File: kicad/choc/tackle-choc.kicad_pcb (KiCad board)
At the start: 2 copper layers, 158 x 119 mm, 114 parts, among them J1 Conn_01x02, SW1 SW_Push, SW10 SW_Push, SW11 SW_Push, SW12 SW_Push, SW13 SW_Push, SW14 SW_Push, SW15 SW_Push, SW16 SW_Push, SW17 SW_Push, SW18 SW_Push, SW19 SW_Push, SW2 SW_Push, SW20 SW_Push, SW21 SW_Push, SW22 SW_Push, SW23 SW_Push, SW24 SW_Push, SW25 SW_Push, SW26 SW_Push, SW27 SW_Push, SW28 SW_Push, SW29 SW_Push, SW3 SW_Push, SW30 SW_Push, SW31 SW_Push, SW32 SW_Push, SW33 SW_Push, SW34 SW_Push, SW35 SW_Push, SW36 SW_Push, SW37 SW_Push, SW38 SW_Push, SW39 SW_Push, SW4 SW_Push, SW40 SW_Push, SW41 SW_Push, SW42 SW_Push, SW43 SW_Push, SW44 SW_Push, SW45 SW_Push, SW46 SW_Push, SW47 SW_Push, SW48 SW_Push, SW5 SW_Push, SW6 SW_Push, SW7 SW_Push, SW8 SW_Push, SW9 SW_Push, U1 nice!nano

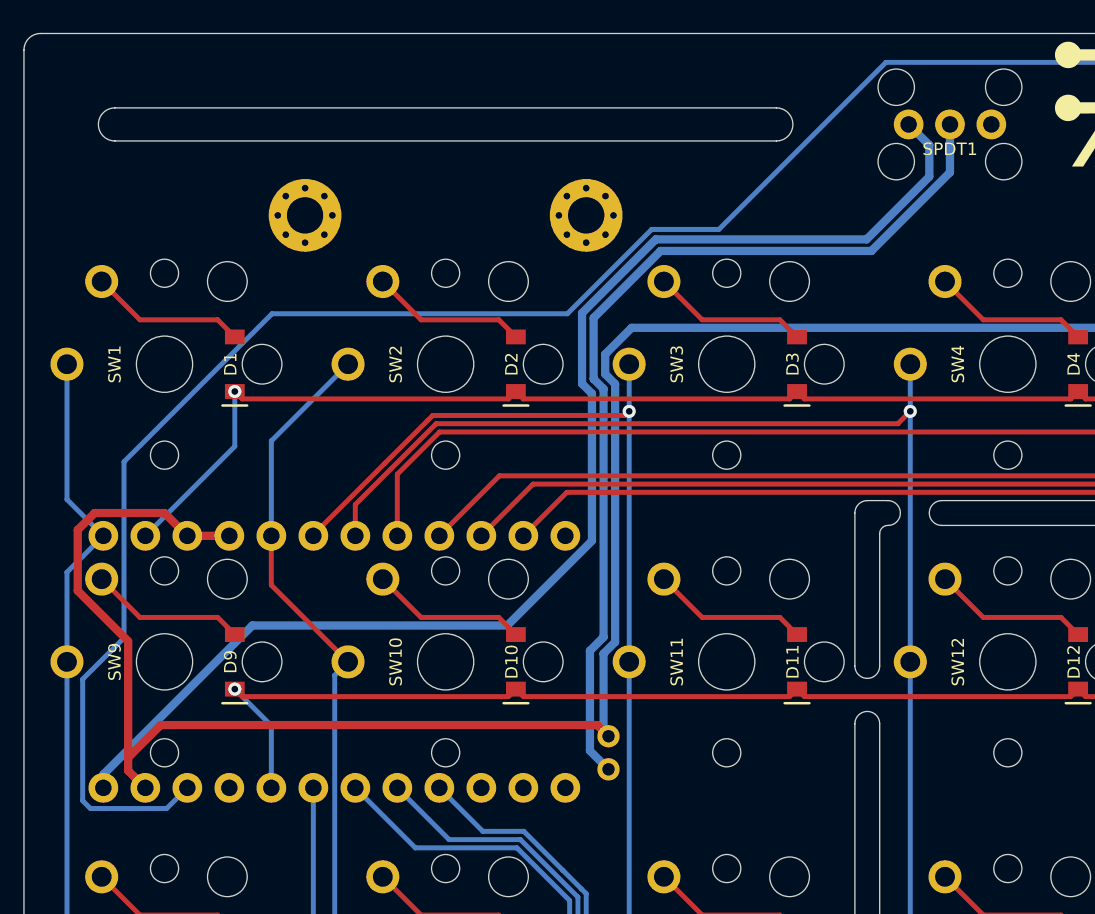
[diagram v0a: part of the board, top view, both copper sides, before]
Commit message: Swap power switch direction, update fabrication settings
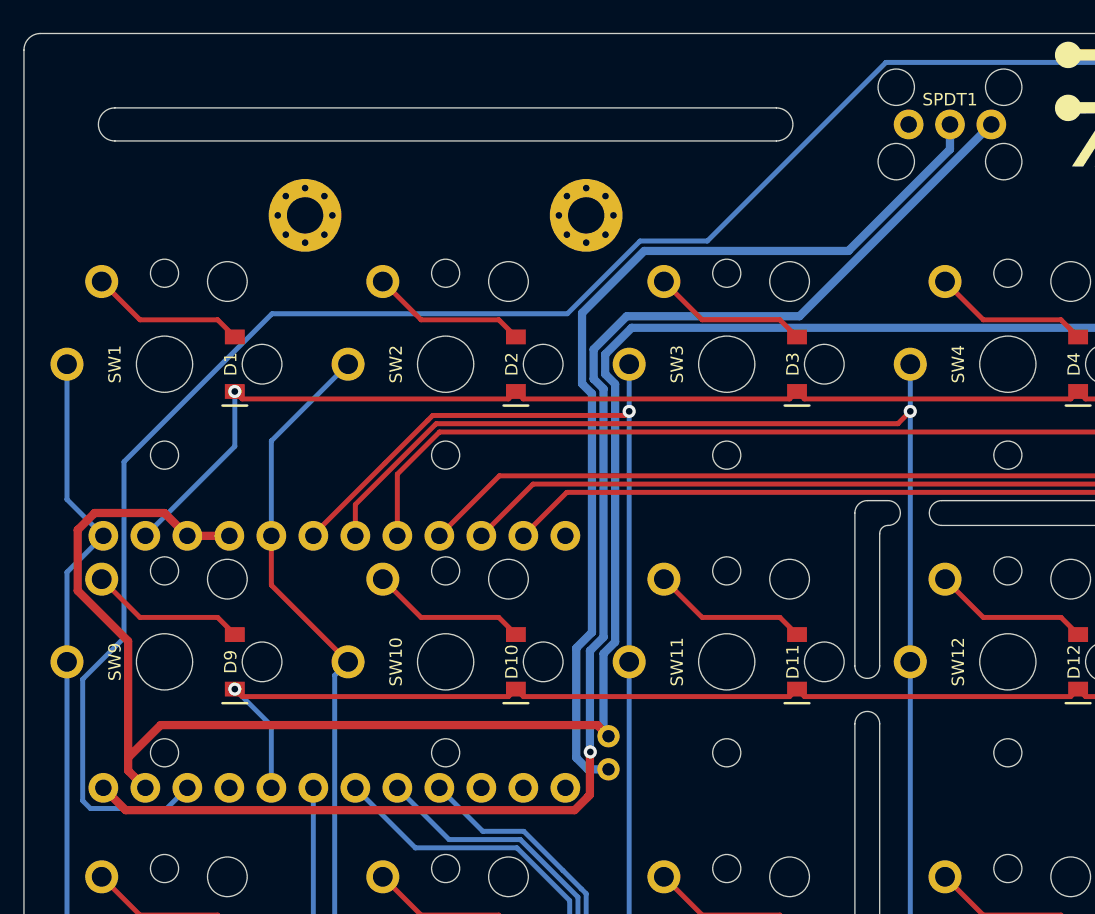
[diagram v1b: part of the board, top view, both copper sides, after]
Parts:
- turned SPDT1 to 180 degrees
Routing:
- net RAW: track 78.3 -> 87.6 mm, vias 0 -> 1
- net BAT+: track 56.5 -> 57.6 mm

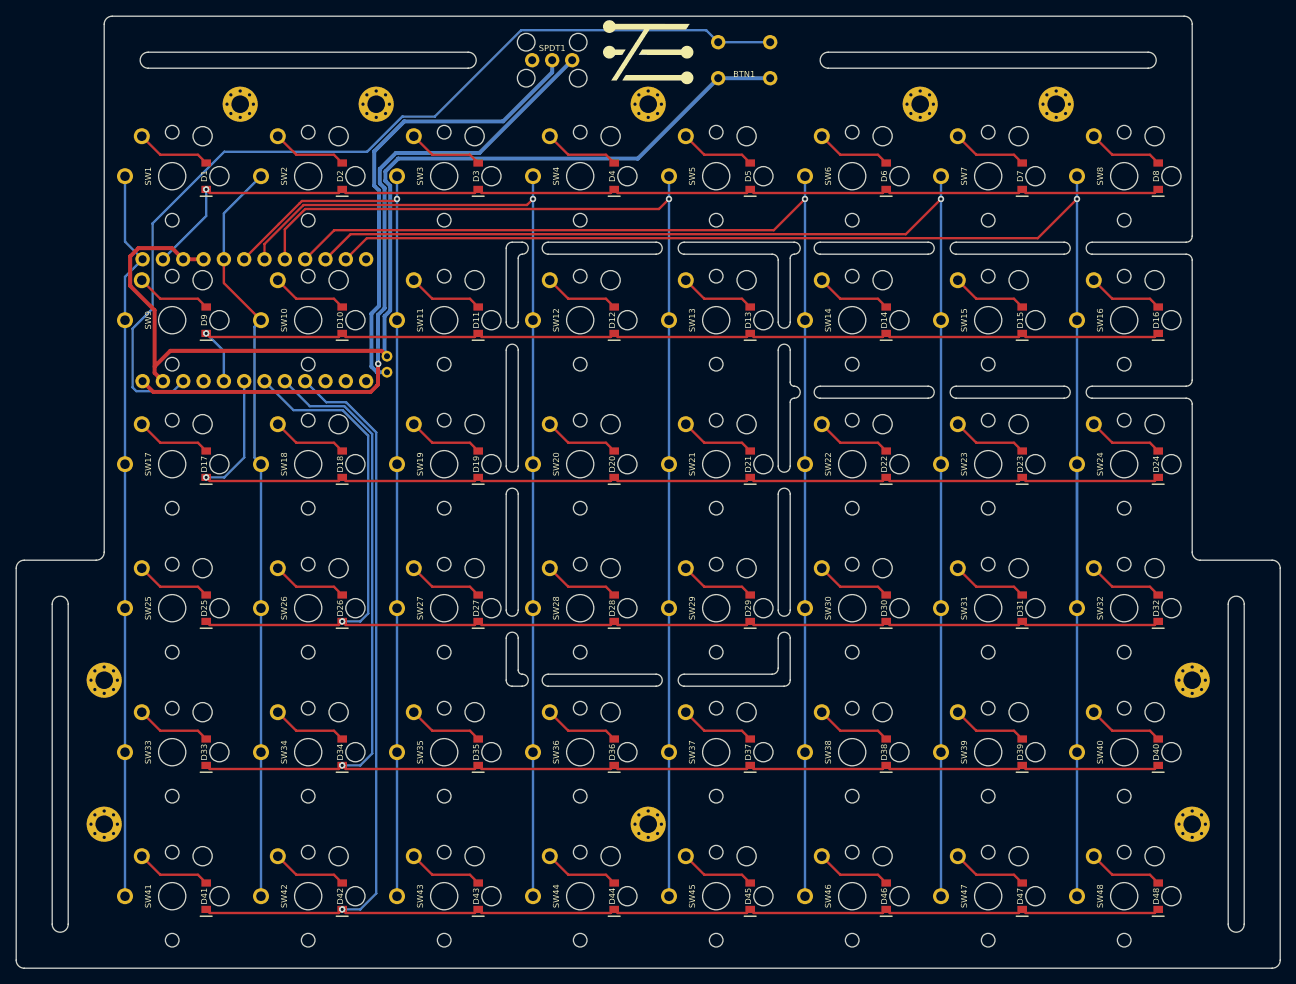
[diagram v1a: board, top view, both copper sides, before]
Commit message: Adjust board cuts and battery connector position
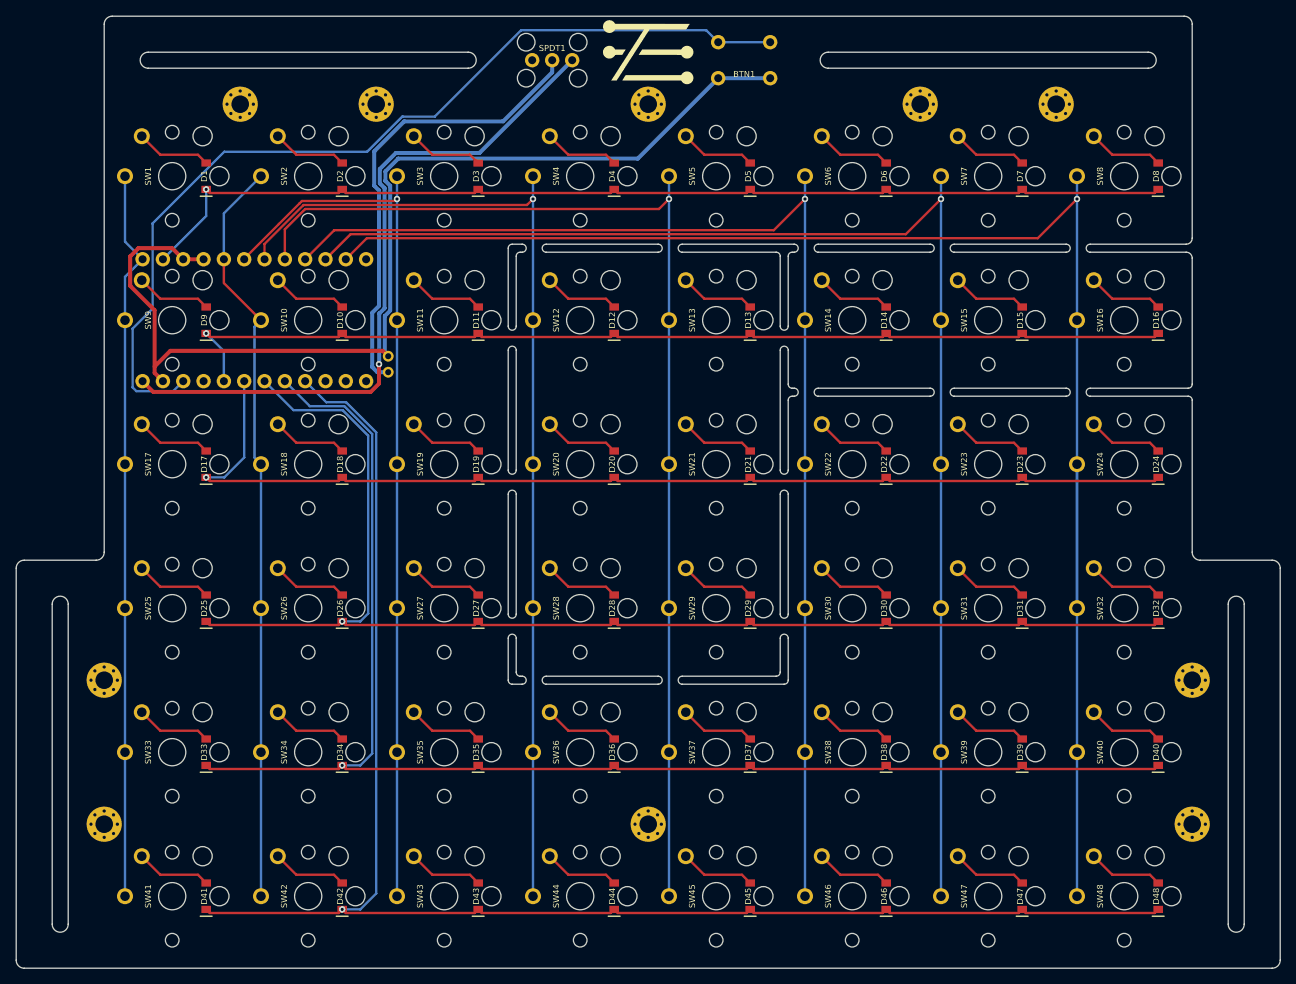
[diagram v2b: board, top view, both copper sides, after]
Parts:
- moved J1 0.15 mm to (114.2, 73.5)
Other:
- outline, holes or cut-outs redrawn

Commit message: Adjust strap slot sizes
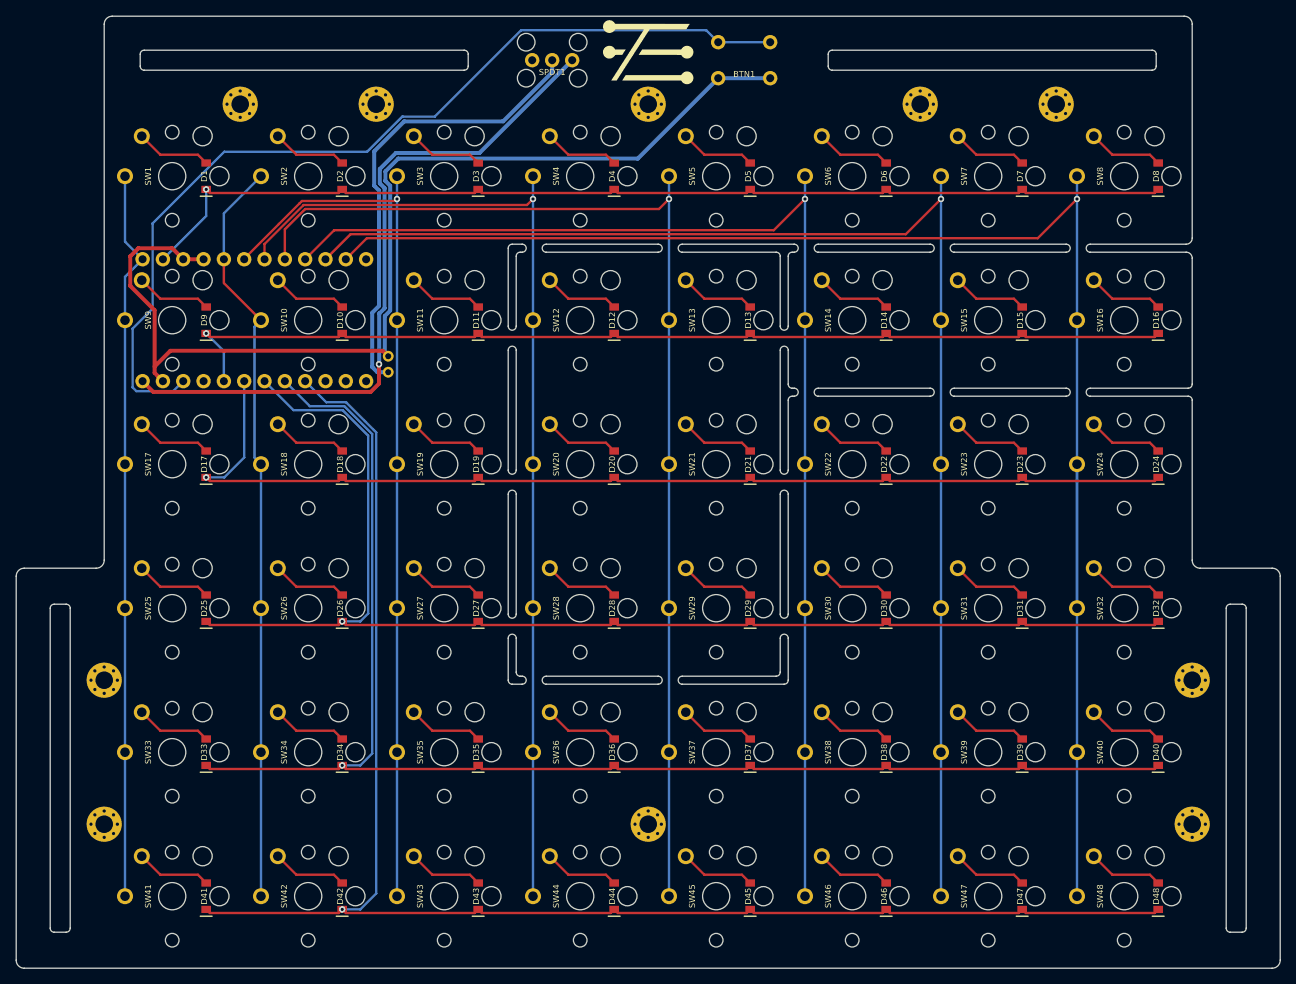
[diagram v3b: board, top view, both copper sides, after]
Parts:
- turned SPDT1 to 0 degrees
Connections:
- SPDT1 pad 1: RAW -> unconnected-(SPDT1-A-Pad1)
- SPDT1 pad 3: unconnected-(SPDT1-C-Pad3) -> RAW
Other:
- outline, holes or cut-outs redrawn

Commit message: 1.1 - widen cutouts to make sawing PCBs easier
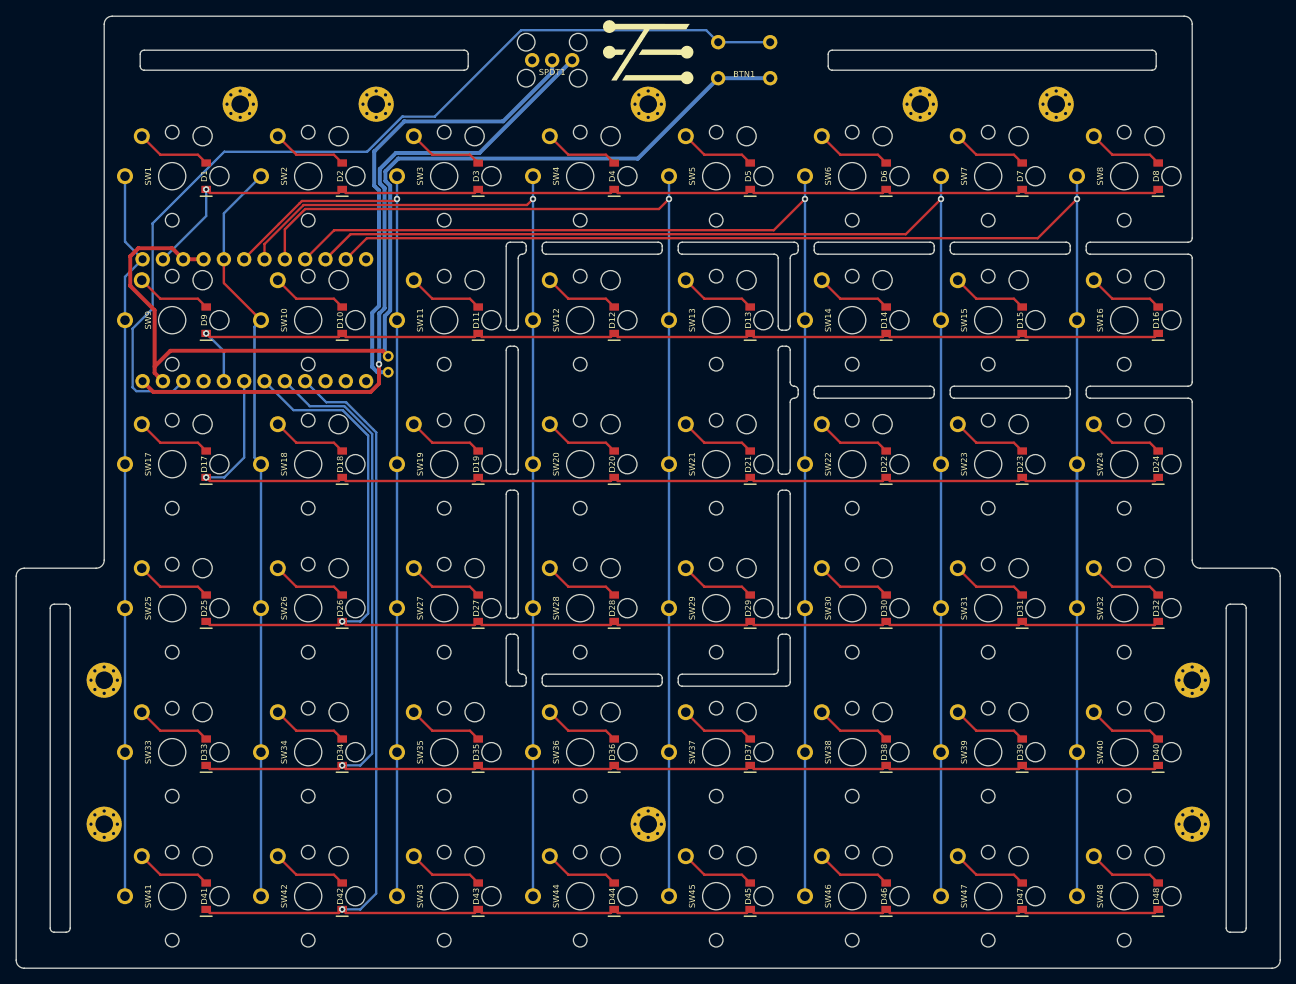
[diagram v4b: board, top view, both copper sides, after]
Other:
- outline, holes or cut-outs redrawn
- board text added: "tackle 1.1"
- board text removed: "tackle 1.0"
